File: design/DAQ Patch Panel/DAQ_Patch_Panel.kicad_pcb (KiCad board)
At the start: 2 copper layers, 83.2 x 118.6 mm, 43 parts, among them J1 Power Terminal 1, J2 Data Output Terminal, J3 Power Terminal 2, J4 Weidmuller LM3RZF

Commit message: ReLayout and Routing in Progress
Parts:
- C3, C4, C6, F1, F2, F3, R10, R11, R12, R13, R15, R17, R5, R6, R7, R8, R9: moved to F.Cu
- moved F2 118.7 mm to (82.8, 28.6), turned to 0 degrees
- moved JP5 117.5 mm to (87.5, 29.4), turned to 0 degrees
- moved R2 94.8 mm to (82.8, 34.5)
- moved JP7 94.7 mm to (89.2, 48.5), turned to 0 degrees
- moved F3 86.2 mm to (82.8, 52.7)
- moved R9 83.5 mm to (82.8, 37.4), turned to 0 degrees
- moved JP9 83.1 mm to (87.5, 53.6)
- moved J1 82.0 mm to (151.2, 57.2), turned to -90 degrees
- moved F1 80.8 mm to (82.8, 76.9)
- moved R10 78.7 mm to (82.8, 40.4)
- moved JP1 77.3 mm to (87.5, 77.7)
- moved R5 72.6 mm to (82.8, 85.7), turned to 0 degrees
- moved JP3 63.3 mm to (89.2, 96.8), turned to 0 degrees
- moved R6 61.3 mm to (82.8, 88.7), turned to 0 degrees
- moved R3 61.1 mm to (82.8, 79.8), turned to 0 degrees
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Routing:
- net /S3IN2: track 34.6 -> 0.00 mm
- net /S2IN2: track 28.3 -> 0.00 mm
- net /S2IN1: track 27.1 -> 0.00 mm
- net /S1IN1: track 17.7 -> 0.00 mm
- net /S3IN1: track 17.5 -> 0.00 mm
- net /S3GND: track 14.2 -> 0.00 mm
- net /S1IN2: track 14.0 -> 0.00 mm
- net /S1GND: track 13.6 -> 0.00 mm
- net /S1DATA1: track 13.1 -> 0.00 mm
- net /S1DATA2: track 12.7 -> 0.00 mm
- net /S3DATA1: track 12.2 -> 0.00 mm
- net /S2GND: track 10.1 -> 0.00 mm
- net /S1POWER: track 9.54 -> 0.00 mm
- net /S3POWER: track 9.36 -> 0.00 mm
- net /S3DATA2: track 9.21 -> 0.00 mm
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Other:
- board outline removed
- board text removed: "First Sub Sheet Grouping"
- board text removed: "Second Sub Sheet Grouping"
- board text removed: "Third Sub Sheet Grouping"

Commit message: More Layout Changes
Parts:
- R1, R10, R13, R14, R15, R16, R2, R3, R4, R5, R6, R9: moved to B.Cu
- moved R15 108.3 mm to (173.4, 120.9), turned to -90 degrees
- moved R13 107.8 mm to (168.2, 121.6), turned to -90 degrees
- moved R10 107.6 mm to (153.0, 121.9), turned to -90 degrees
- moved R16 99.7 mm to (173.4, 106.1), turned to 90 degrees
- moved R9 97.5 mm to (152.9, 105.2), turned to 90 degrees
- moved R14 97.4 mm to (168.2, 105.7), turned to 90 degrees
- moved R2 95.8 mm to (147.8, 104.9), turned to 90 degrees
- moved JP9 91.7 mm to (171.2, 91.1)
- moved JP5 88.2 mm to (151.0, 90.7)
- moved R5 87.8 mm to (162.9, 121.8), turned to -90 degrees
- moved R3 86.0 mm to (157.8, 121.9), turned to -90 degrees
- moved R6 81.9 mm to (163.0, 105.6), turned to 90 degrees
- moved R4 78.5 mm to (158.0, 105.5), turned to 90 degrees
- moved JP1 74.4 mm to (160.9, 90.5)
- moved R1 21.5 mm to (147.8, 121.9), turned to -90 degrees
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
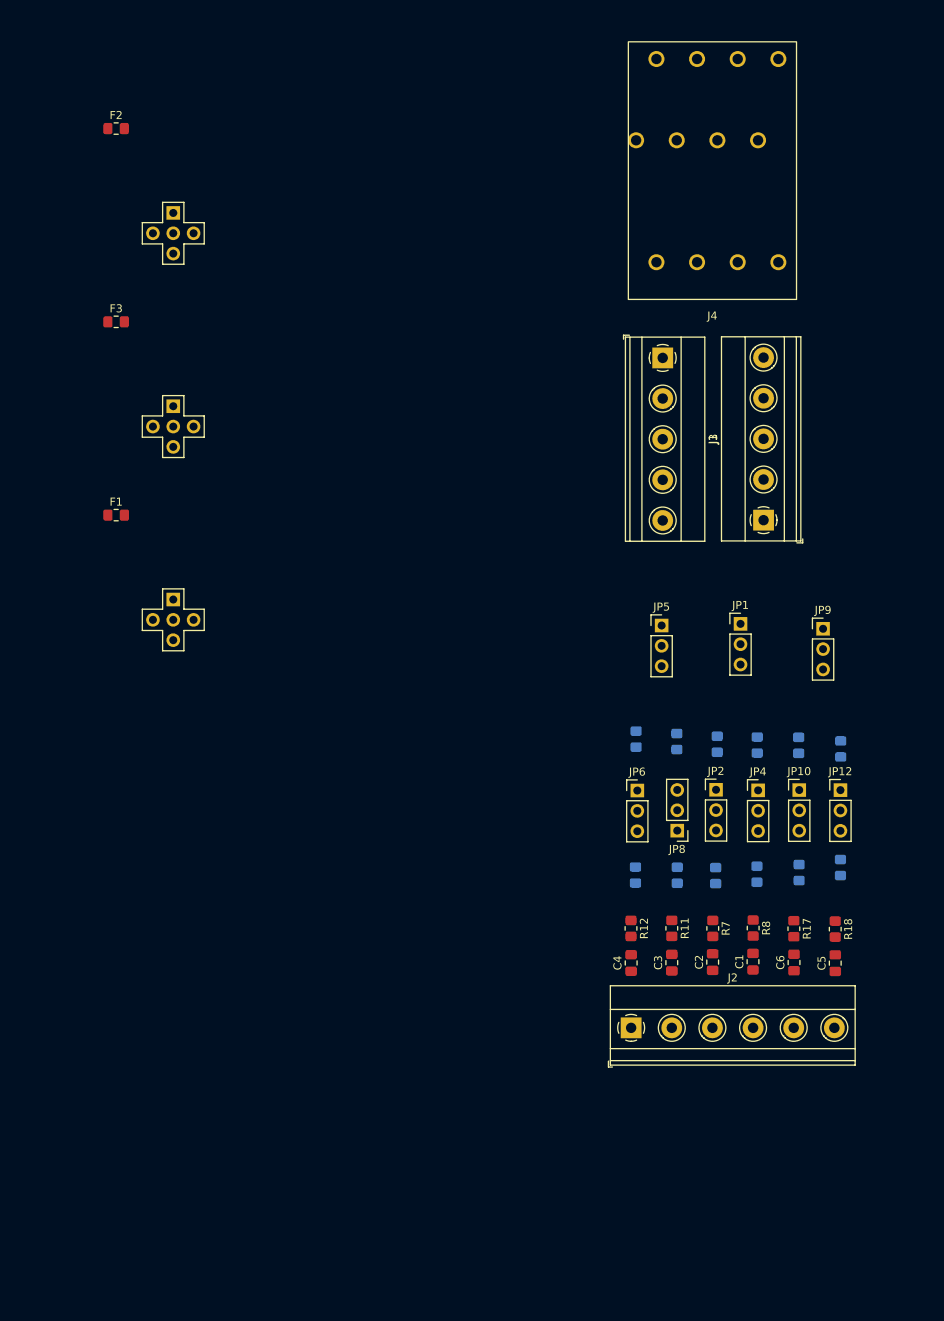
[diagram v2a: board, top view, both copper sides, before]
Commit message: Second Try at Routing (Cleanup Needed)
Alternate Routing of Traces, needs to input pours and simplification
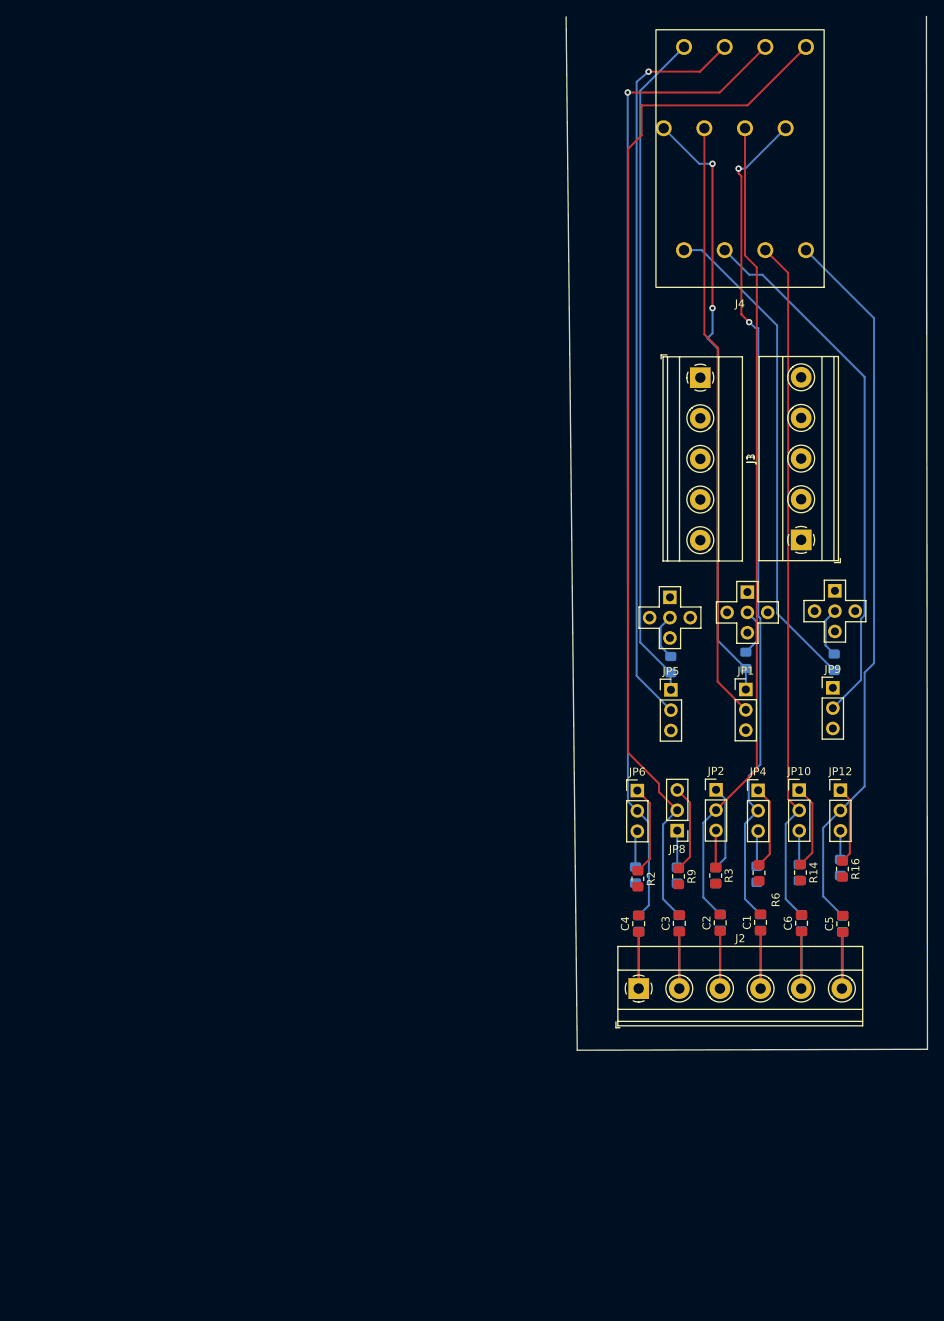
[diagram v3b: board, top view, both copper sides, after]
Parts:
- F1, F2, F3, R11, R12, R17, R18, R7, R8: moved to B.Cu
- R14, R16, R2, R3, R6, R9: moved to F.Cu
- moved F3 99.3 mm to (172.6, 95.3), turned to 90 degrees
- moved F2 96.4 mm to (152.2, 95.6), turned to 90 degrees
- moved JP11 85.9 mm to (171.9, 95.7)
- moved F1 80.8 mm to (161.6, 95.0), turned to 90 degrees
- moved JP7 78.5 mm to (151.3, 96.5)
- moved JP3 71.8 mm to (161.0, 95.9)
- moved R2 17.5 mm to (148.1, 122.3), turned to -90 degrees
- moved R9 16.9 mm to (153.1, 122.0), turned to -90 degrees
- moved R4 16.4 mm to (157.8, 121.9), turned to -90 degrees
- moved R6 16.0 mm to (163.2, 121.6), turned to -90 degrees
- moved R14 15.9 mm to (168.4, 121.6), turned to -90 degrees
- moved R16 15.0 mm to (173.6, 121.1), turned to -90 degrees
- moved JP1 8.23 mm to (161.6, 98.7)
- moved JP5 8.12 mm to (152.2, 98.7)
- moved JP9 7.48 mm to (172.4, 98.5)
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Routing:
- net /S1IN2: track 0.00 -> 129.6 mm
- net /S1IN1: track 0.00 -> 124.1 mm, vias 0 -> 1
- net /S2IN2: track 0.00 -> 105.4 mm, vias 0 -> 2
- net /S2IN1: track 0.00 -> 102.5 mm
- net /S1GND: track 0.00 -> 93.1 mm, vias 0 -> 1
- net /S3IN2: track 0.00 -> 90.4 mm
- net /S3IN1: track 0.00 -> 86.4 mm
- net /S1POWER: track 0.00 -> 84.2 mm
- net /S2POWER: track 0.00 -> 76.6 mm, vias 0 -> 2
- net /S2GND: track 0.00 -> 74.8 mm
- net /S3GND: track 0.00 -> 67.1 mm
- net /S3POWER: track 0.00 -> 61.6 mm
- net /S2DATA2: track 0.00 -> 14.5 mm
- net /S2DATA1: track 0.00 -> 14.5 mm
- net /S3DATA1: track 0.00 -> 14.4 mm
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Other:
- board outline added: 45.2 x 129.2 mm

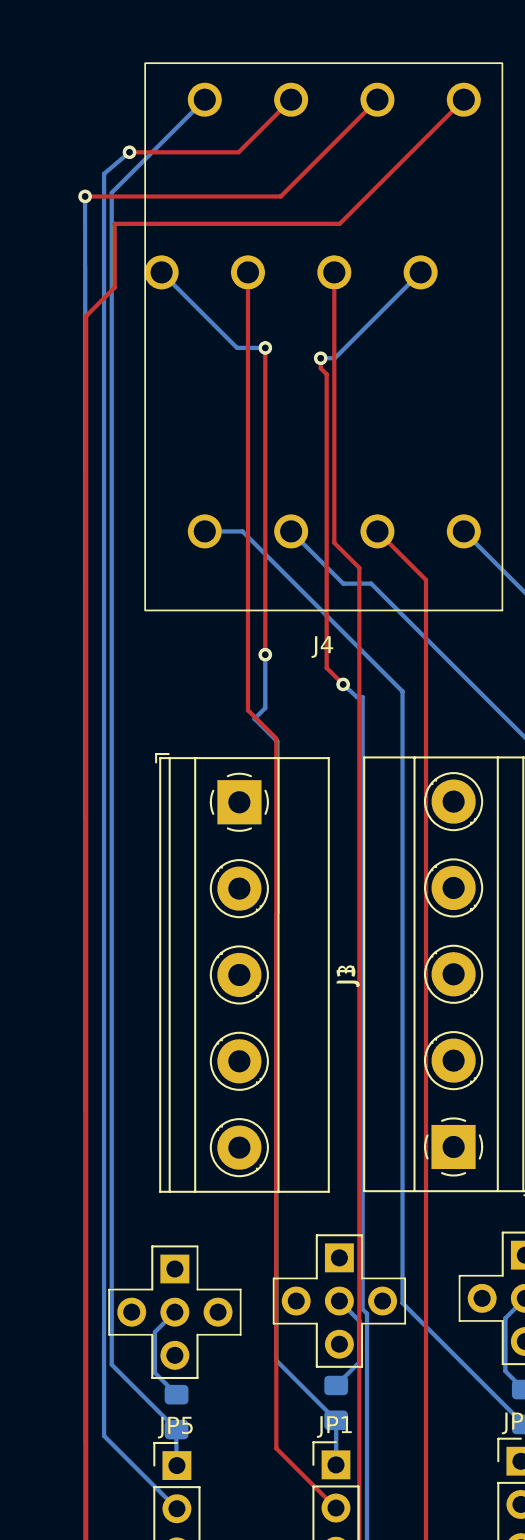
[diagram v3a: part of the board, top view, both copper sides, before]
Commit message: 2 Vias Removed
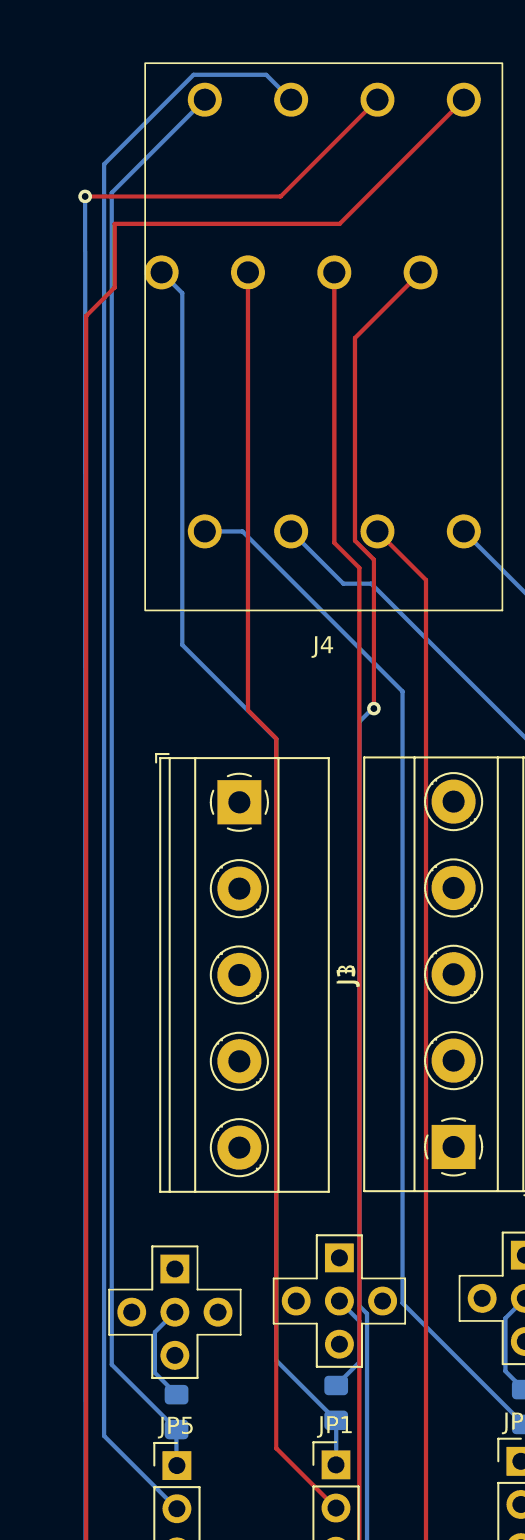
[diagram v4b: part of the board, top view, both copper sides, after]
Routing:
- net /S2IN2: track 105.4 -> 103.7 mm, vias 2 -> 1
- net /S2POWER: track 76.6 -> 75.0 mm, vias 2 -> 0
- net /S1GND: track 93.1 -> 94.7 mm, vias 1 -> 0
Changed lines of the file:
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@@
   (segment (start 168.52 136.02) (end 168.48 136.06) (width 0.25) (layer "B.Cu") (net 7))
   (segment (start 168.52 128.86) (end 168.52 136.02) (width 0.25) (layer "B.Cu") (net 7))
-  (segment (start 157.39 51.01) (end 157.39 33.02) (width 0.25) (layer "F.Cu") (net 8))
-  (segment (start 157.39 33.02) (end 157.39 33.02) (width 0.25) (layer "F.Cu") (net 8))
-  (segment (start 157.39 32.96) (end 157.33 32.96) (width 0.25) (layer "F.Cu") (net 8))
-  (segment (start 157.39 33.02) (end 157.39 32.96) (width 0.25) (layer "F.Cu") (net 8))
-  (via (at 157.39 51.01) (size 0.8) (drill 0.4) (layers "F.Cu" "B.Cu") (net 8))
-  (via (at 157.39 32.96) (size 0.8) (drill 0.4) (layers "F.Cu" "B.Cu") (net 8))
+  (segment (start 161.56 96.06) (end 158.035 92.535) (width 0.25) (layer "B.Cu") (net 8))
   (segment (start 161.56 96.06) (end 161.56 98.67) (width 0.25) (layer "B.Cu") (net 8))
   (segment (start 161.56 98.67) (end 161.55 98.68) (width 0.25) (layer "B.Cu") (net 8))
-  (segment (start 158.035 66.285) (end 158.1 66.22) (width 0.25) (layer "B.Cu") (net 8))
-  (segment (start 161.56 96.06) (end 158.035 92.535) (width 0.25) (layer "B.Cu") (net 8))
-  (segment (start 156.76 54.78) (end 157.39 54.15) (width 0.25) (layer "B.Cu") (net 8))
-  (segment (start 158.1 56.12) (end 156.76 54.78) (width 0.25) (layer "B.Cu") (net 8))
-  (segment (start 157.39 51.01) (end 157.39 51.07) (width 0.25) (layer "B.Cu") (net 8))
-  (segment (start 155.7325 32.96) (end 151.29 28.5175) (width 0.25) (layer "B.Cu") (net 8))
-  (segment (start 158.1 66.22) (end 158.1 56.12) (width 0.25) (layer "B.Cu") (net 8))
-  (segment (start 157.39 32.96) (end 155.7325 32.96) (width 0.25) (layer "B.Cu") (net 8))
-  (segment (start 158.035 92.535) (end 158.035 66.285) (width 0.25) (layer "B.Cu") (net 8))
+  (segment (start 152.505 50.435) (end 152.505 29.7325) (width 0.25) (layer "B.Cu") (net 8))
+  (segment (start 158.035 55.965) (end 152.505 50.435) (width 0.25) (layer "B.Cu") (net 8))
+  (segment (start 152.505 29.7325) (end 151.29 28.5175) (width 0.25) (layer "B.Cu") (net 8))
   (segment (start 151.29 28.5175) (end 150.895 28.9125) (width 0.25) (layer "B.Cu") (net 8))
-  (segment (start 157.39 54.15) (end 157.39 51.01) (width 0.25) (layer "B.Cu") (net 8))
+  (segment (start 158.035 92.535) (end 158.035 55.965) (width 0.25) (layer "B.Cu") (net 8))
   (segment (start 162.925 90.215) (end 161.75 89.04) (width 0.25) (layer "B.Cu") (net 9))
   (segment (start 161.56 94.01) (end 162.925 92.645) (width 0.25) (layer "B.Cu") (net 9))
@@
   (segment (start 151.21 124.88) (end 153.23 126.9) (width 0.25) (layer "B.Cu") (net 19))
   (segment (start 151.21 115.545) (end 151.21 124.88) (width 0.25) (layer "B.Cu") (net 19))
-  (segment (start 149.4 21.45) (end 155.8175 21.45) (width 0.25) (layer "F.Cu") (net 20))
-  (segment (start 155.8175 21.45) (end 158.91 18.3575) (width 0.25) (layer "F.Cu") (net 20))
-  (via (at 149.4 21.45) (size 0.8) (drill 0.4) (layers "F.Cu" "B.Cu") (net 20))
-  (segment (start 147.905 96.975) (end 147.905 22.715) (width 0.25) (layer "B.Cu") (net 20))
-  (segment (start 147.905 22.715) (end 149.4 21.45) (width 0.25) (layer "B.Cu") (net 20))
+  (segment (start 157.4425 16.89) (end 153.17 16.89) (width 0.25) (layer "B.Cu") (net 20))
+  (segment (start 147.905 96.975) (end 147.905 22.155) (width 0.25) (layer "B.Cu") (net 20))
   (segment (start 152.19 101.26) (end 147.905 96.975) (width 0.25) (layer "B.Cu") (net 20))
+  (segment (start 147.905 22.155) (end 153.17 16.89) (width 0.25) (layer "B.Cu") (net 20))
+  (segment (start 158.91 18.3575) (end 157.4425 16.89) (width 0.25) (layer "B.Cu") (net 20))
   (segment (start 161.45 44.43) (end 162.925 45.905) (width 0.25) (layer "F.Cu") (net 21))
   (segment (start 162.925 45.905) (end 162.925 108.66) (width 0.25) (layer "F.Cu") (net 21))
@@
   (segment (start 156.24 124.67) (end 158.36 126.79) (width 0.25) (layer "B.Cu") (net 21))
   (segment (start 156.24 115.345) (end 156.24 124.67) (width 0.25) (layer "B.Cu") (net 21))
-  (segment (start 161 34.51) (end 160.65 34.16) (width 0.25) (layer "F.Cu") (net 22))
-  (segment (start 160.65 33.57) (end 160.65 33.74) (width 0.25) (layer "F.Cu") (net 22))
-  (segment (start 161.97 52.76) (end 161 51.79) (width 0.25) (layer "F.Cu") (net 22))
-  (segment (start 160.65 34.16) (end 160.65 33.57) (width 0.25) (layer "F.Cu") (net 22))
-  (segment (start 161 51.79) (end 161 34.51) (width 0.25) (layer "F.Cu") (net 22))
-  (via (at 160.65 33.57) (size 0.8) (drill 0.4) (layers "F.Cu" "B.Cu") (net 22))
-  (via (at 161.97 52.76) (size 0.8) (drill 0.4) (layers "F.Cu" "B.Cu") (net 22))
-  (segment (start 161.97 52.76) (end 162.105 52.825) (width 0.25) (layer "B.Cu") (net 22))
+  (segment (start 162.665 32.3825) (end 166.53 28.5175) (width 0.25) (layer "F.Cu") (net 22))
+  (segment (start 163.78 45.421334) (end 162.665 44.306334) (width 0.25) (layer "F.Cu") (net 22))
+  (segment (start 163.78 54.18) (end 163.78 45.421334) (width 0.25) (layer "F.Cu") (net 22))
+  (segment (start 162.665 44.306334) (end 162.665 32.3825) (width 0.25) (layer "F.Cu") (net 22))
+  (via (at 163.78 54.18) (size 0.8) (drill 0.4) (layers "F.Cu" "B.Cu") (net 22))
+  (segment (start 163.09 113.825) (end 161.915 112.65) (width 0.25) (layer "B.Cu") (net 22))
+  (segment (start 161.915 112.65) (end 161.915 109.505) (width 0.25) (layer "B.Cu") (net 22))
+  (segment (start 163.78 54.18) (end 163.78 54.1) (width 0.25) (layer "B.Cu") (net 22))
+  (segment (start 163.375 89.785054) (end 162.925 89.335054) (width 0.25) (layer "B.Cu") (net 22))
+  (segment (start 163.78 54.1) (end 163.7 54.18) (width 0.25) (layer "B.Cu") (net 22))
+  (segment (start 161.45 115.465) (end 163.09 113.825) (width 0.25) (layer "B.Cu") (net 22))
+  (segment (start 161.915 109.505) (end 163.375 108.045) (width 0.25) (layer "B.Cu") (net 22))
+  (segment (start 161.45 115.465) (end 161.45 124.86) (width 0.25) (layer "B.Cu") (net 22))
+  (segment (start 162.925 89.335054) (end 162.925 54.955) (width 0.25) (layer "B.Cu") (net 22))
+  (segment (start 162.925 54.955) (end 163.7 54.18) (width 0.25) (layer "B.Cu") (net 22))
+  (segment (start 161.45 124.86) (end 163.39 126.8) (width 0.25) (layer "B.Cu") (net 22))
   (segment (start 163.375 108.045) (end 163.375 89.785054) (width 0.25) (layer "B.Cu") (net 22))
-  (segment (start 161.915 109.505) (end 163.375 108.045) (width 0.25) (layer "B.Cu") (net 22))
-  (segment (start 160.65 33.57) (end 161.4775 33.57) (width 0.25) (layer "B.Cu") (net 22))
-  (segment (start 163.09 113.825) (end 161.915 112.65) (width 0.25) (layer "B.Cu") (net 22))
-  (segment (start 163.375 89.785054) (end 163.115 89.525054) (width 0.25) (layer "B.Cu") (net 22))
-  (segment (start 161.4775 33.57) (end 166.53 28.5175) (width 0.25) (layer "B.Cu") (net 22))
-  (segment (start 161.45 115.465) (end 163.09 113.825) (width 0.25) (layer "B.Cu") (net 22))
-  (segment (start 161.45 115.465) (end 161.45 124.86) (width 0.25) (layer "B.Cu") (net 22))
-  (segment (start 163.115 89.525054) (end 163.115 53.505) (width 0.25) (layer "B.Cu") (net 22))
-  (segment (start 162.785 53.505) (end 161.97 52.76) (width 0.25) (layer "B.Cu") (net 22))
-  (segment (start 163.115 53.505) (end 162.785 53.505) (width 0.25) (layer "B.Cu") (net 22))
-  (segment (start 161.45 124.86) (end 163.39 126.8) (width 0.25) (layer "B.Cu") (net 22))
-  (segment (start 161.915 112.65) (end 161.915 109.505) (width 0.25) (layer "B.Cu") (net 22))
+  (segment (start 163.7 54.18) (end 163.78 54.18) (width 0.25) (layer "B.Cu") (net 22))
   (segment (start 161.55 101.22) (end 158.035 97.705) (width 0.25) (layer "F.Cu") (net 23))
   (segment (start 158.035 97.705) (end 158.035 55.945) (width 0.25) (layer "F.Cu") (net 23))

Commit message: More Changes
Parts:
- moved C3 39.9 mm to (128.9, 159.6)
- moved C6 39.9 mm to (144.2, 159.6)
- moved F1 39.9 mm to (137.3, 126.7)
- moved J3 39.9 mm to (144.2, 111.6)
- moved JP7 39.9 mm to (127.0, 128.2)
- moved R17 39.9 mm to (144.2, 159.5)
- moved R5 39.9 mm to (138.6, 153.4)
- moved R7 39.9 mm to (134.1, 159.5)
- moved C4 39.9 mm to (123.9, 159.6)
- moved J1 39.9 mm to (131.6, 91.4)
- moved J4 39.9 mm to (136.5, 88.0)
- moved JP1 39.9 mm to (137.2, 130.3)
- moved JP2 39.9 mm to (133.5, 142.9)
- moved JP4 39.9 mm to (138.8, 143.0)
- moved JP6 39.9 mm to (123.7, 143.0)
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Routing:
- net /S2IN2: track 103.7 -> 104.6 mm, vias 1 -> 0
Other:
- board size 45.2 x 129.2 mm -> 43.8 x 129.3 mm
